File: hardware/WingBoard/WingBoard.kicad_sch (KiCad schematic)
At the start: 12 parts

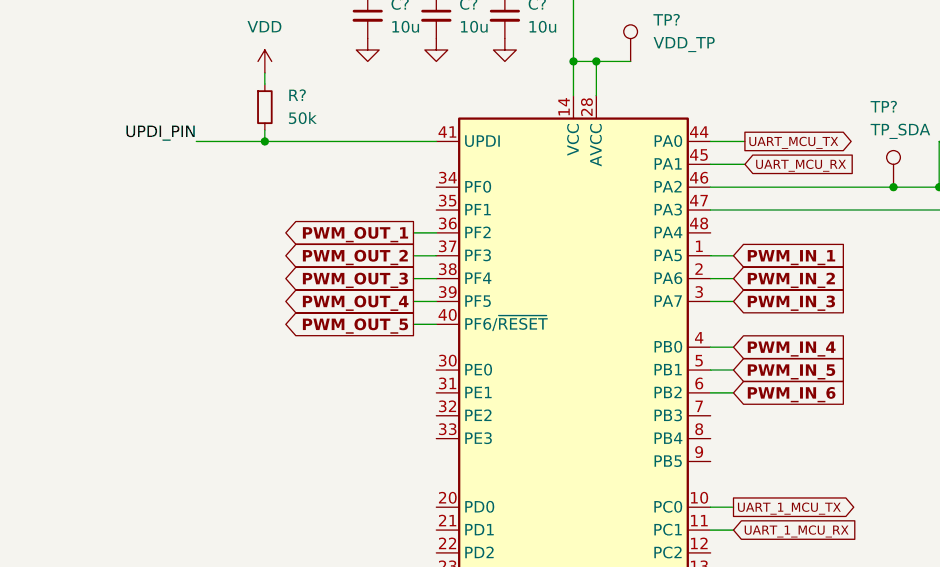
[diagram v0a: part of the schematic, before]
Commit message: Added extra I2C headers to the schematic.
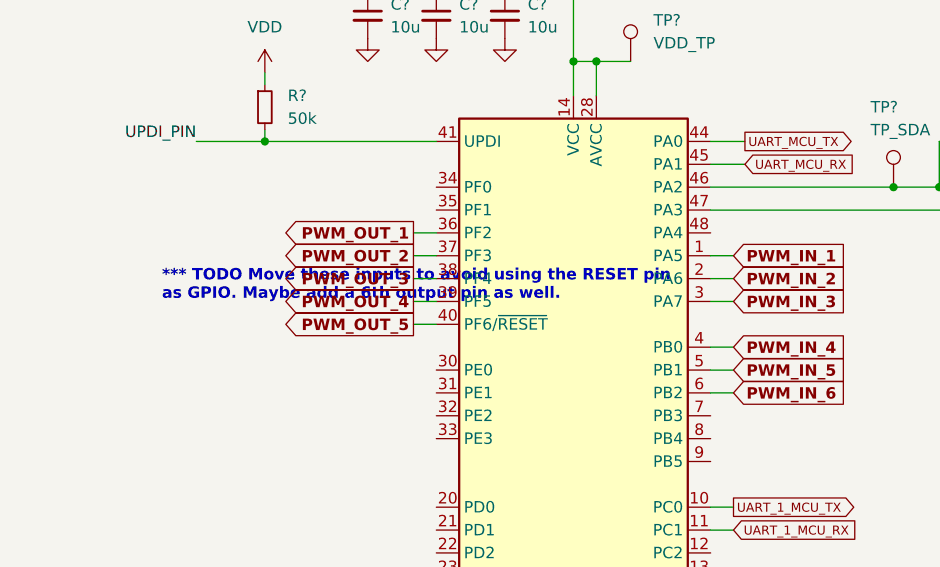
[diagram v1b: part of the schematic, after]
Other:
- note added: "*** TODO Move these inputs to avoid using the RESET pin as GPIO. Maybe add a 6th output pin as well."
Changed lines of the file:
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@@
     (effects (font (size 2 2) bold) (justify left bottom))
+  )
+  (text "*** TODO Move these inputs to avoid using the RESET pin \nas GPIO. Maybe add a 6th output pin as well. "
+    (at 111.76 90.17 0)
+    (effects (font (size 1.27 1.27) bold) (justify left bottom))
   )
   (label "UPDI_PIN" (at 115.57 72.39 180)
@@
       (reference "#PWR?") (unit 1) (value "VDD") (footprint "")
     )
+    (path "/65d0734d-0a9b-4de3-a1fd-6529edb3e633/6a814641-d20c-418e-bbf6-ee1c84b98cad"
+      (reference "#PWR?") (unit 1) (value "VDD") (footprint "")
+    )
     (path "/7d003a0c-bec3-4bcf-bfcd-49935645a638/6fb03914-ff97-4a61-9273-9addb35c7176"
       (reference "#PWR?") (unit 1) (value "VDD") (footprint "")
@@
       (reference "#PWR?") (unit 1) (value "GND") (footprint "")
     )
+    (path "/65d0734d-0a9b-4de3-a1fd-6529edb3e633/caa19d0f-3ce8-416e-bb63-fc48f119bca8"
+      (reference "#PWR?") (unit 1) (value "GND") (footprint "")
+    )
+    (path "/65d0734d-0a9b-4de3-a1fd-6529edb3e633/ccb53472-8d23-471d-b2ec-caf44c144929"
+      (reference "#PWR?") (unit 1) (value "+3.3V") (footprint "")
+    )
+    (path "/65d0734d-0a9b-4de3-a1fd-6529edb3e633/d00ec237-131f-4e59-a480-f807d62e1309"
+      (reference "#PWR?") (unit 1) (value "GND") (footprint "")
+    )
     (path "/4e596909-8b66-4241-be1c-98ec74d77d36/d23c6e59-cc6d-468e-8847-c3cbf6d7174c"
       (reference "#PWR?") (unit 1) (value "GND") (footprint "")
@@
       (reference "J?") (unit 1) (value "PWM_IN2") (footprint "")
     )
+    (path "/65d0734d-0a9b-4de3-a1fd-6529edb3e633/5cc5677a-8af6-4030-9d19-2ee131f6671a"
+      (reference "J?") (unit 1) (value "I2C_X_5V") (footprint "")
+    )
     (path "/4e596909-8b66-4241-be1c-98ec74d77d36/814f2db9-0947-4f62-a212-136e66c5dfa2"
       (reference "J?") (unit 1) (value "PWM_IN1") (footprint "")
@@
       (reference "J?") (unit 1) (value "PWM_IN3") (footprint "")
     )
+    (path "/65d0734d-0a9b-4de3-a1fd-6529edb3e633/f9357d31-2708-45a1-b765-33a95a94766e"
+      (reference "J?") (unit 1) (value "I2C_X_5V") (footprint "")
+    )
     (path "/fd764008-cb4d-4b17-a97c-334a95d80dd4"

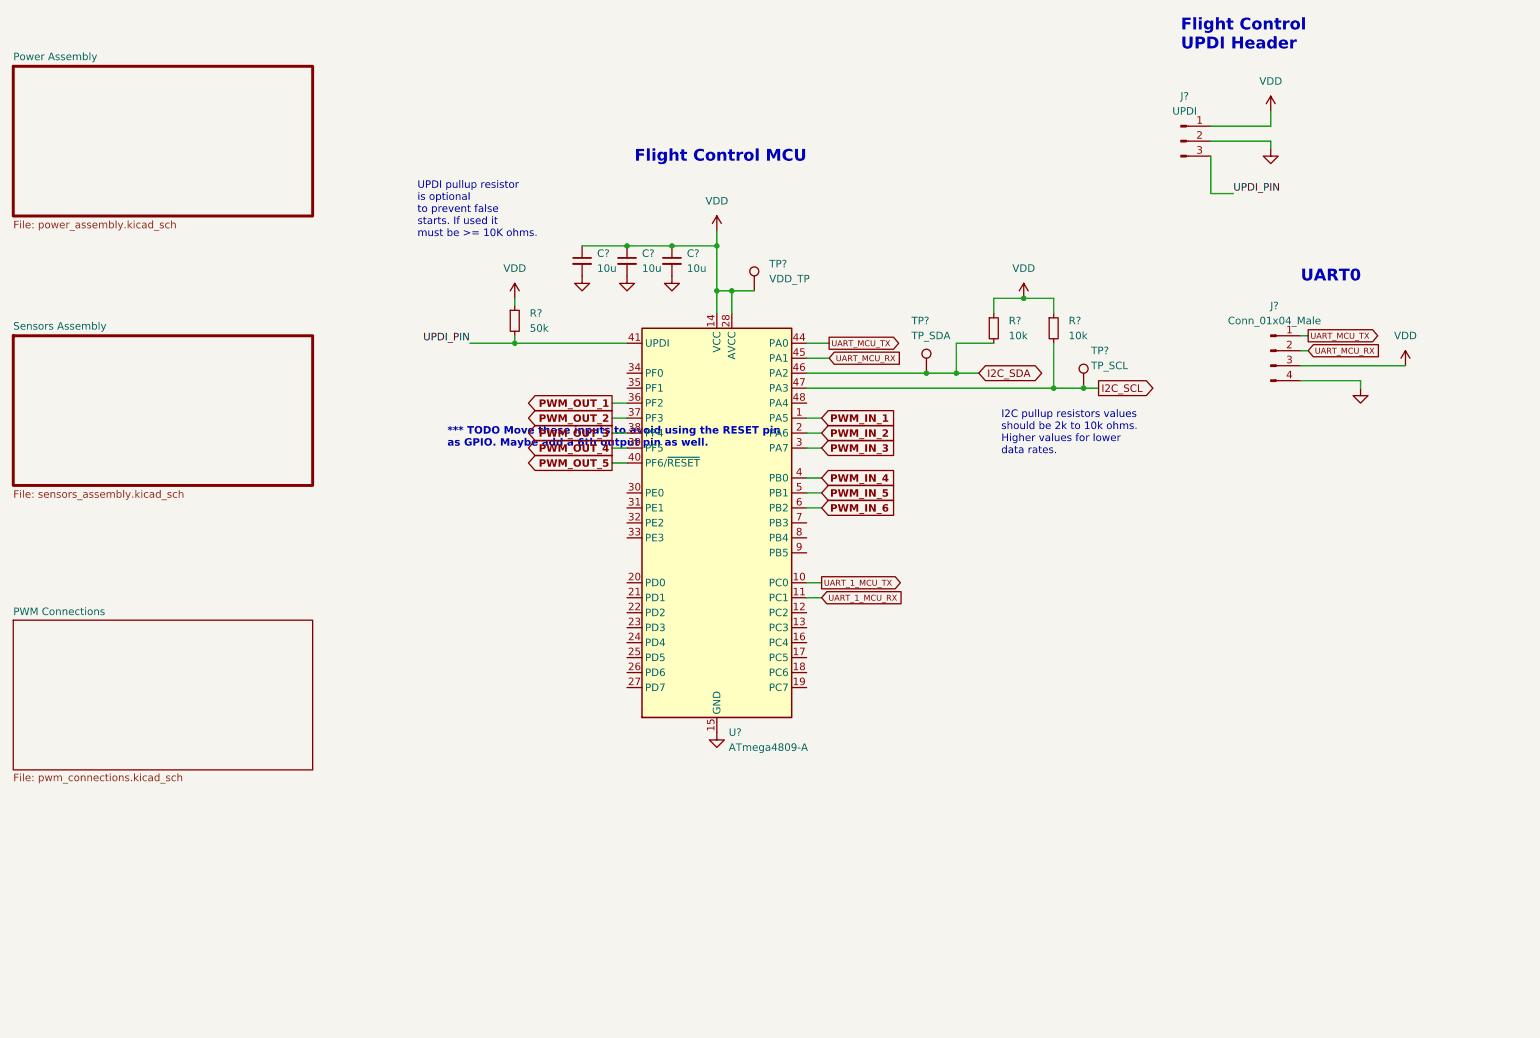
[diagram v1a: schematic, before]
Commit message: Added pwm controller.
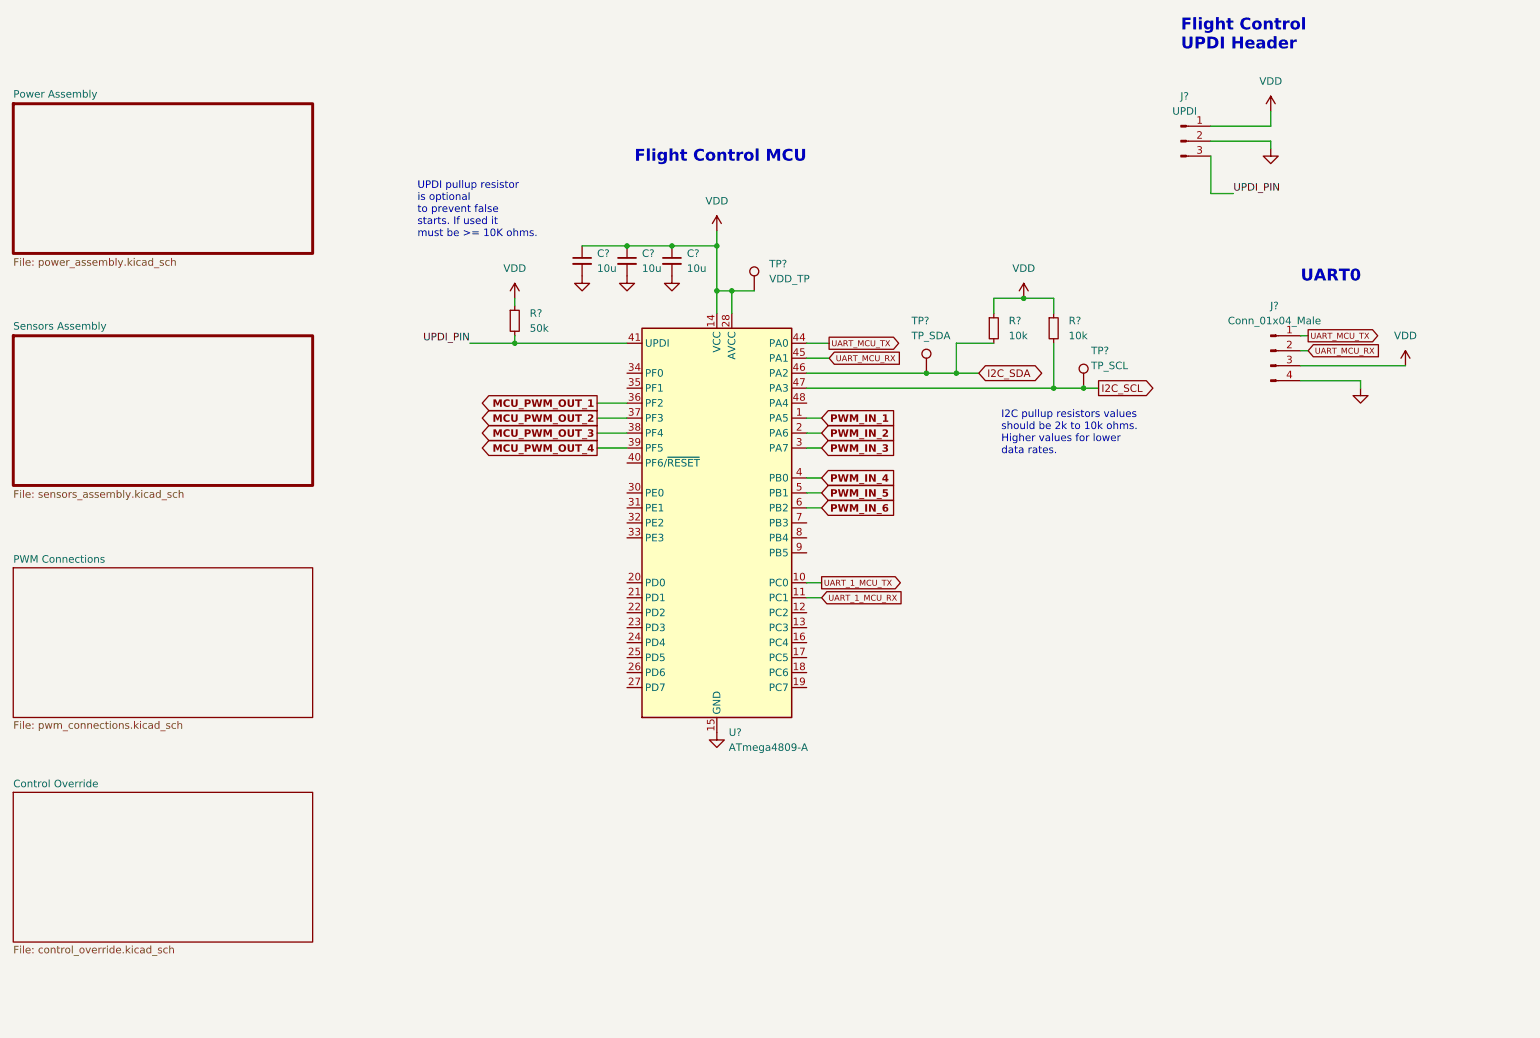
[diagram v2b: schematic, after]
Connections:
- net PWM_OUT_1 renamed MCU_PWM_OUT_1
- net PWM_OUT_2 renamed MCU_PWM_OUT_2
- net PWM_OUT_3 renamed MCU_PWM_OUT_3
- net PWM_OUT_4 renamed MCU_PWM_OUT_4
- net PWM_OUT_5: no longer names the net of U?.40 (PF6/~{RESET})
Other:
- added sheet Control Override (control_override.kicad_sch)
- note removed: "*** TODO Move these inputs to avoid using the RESET pin as GPIO. Maybe add a 6th output pin as well."

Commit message: Hardware update: status LEDs, DIP switches, & test points.
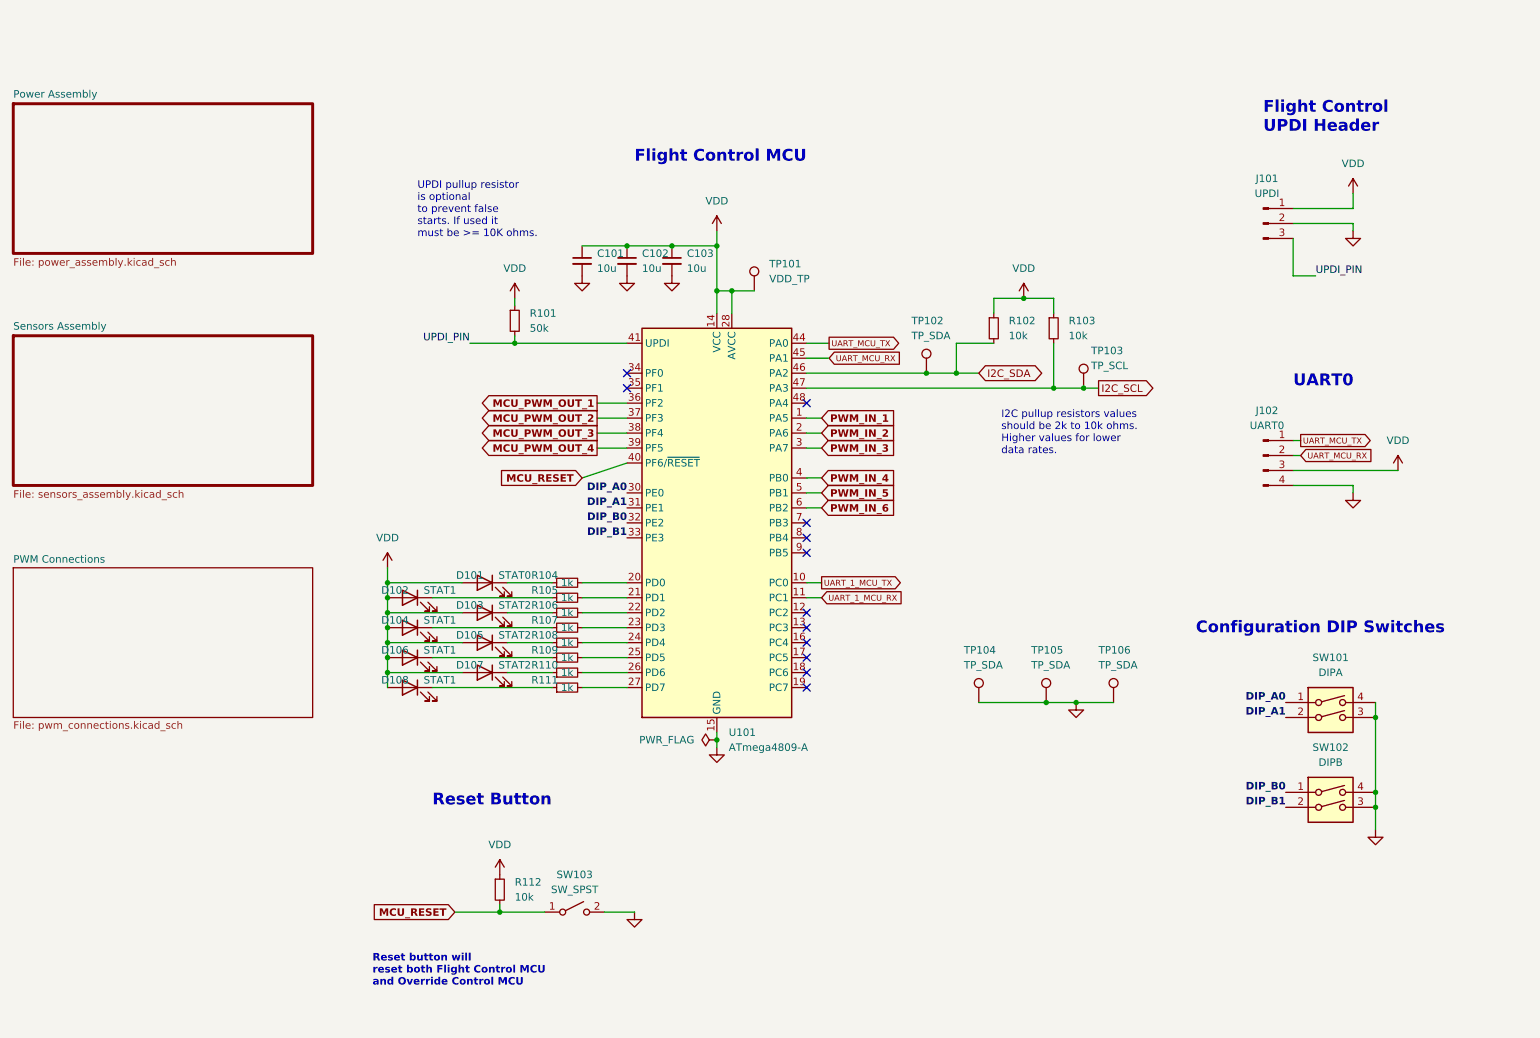
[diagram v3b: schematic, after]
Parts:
- added D101: STAT0, symbol Device:LED
- added D102, D104, D106, D108: STAT1, symbol Device:LED
- added D103, D105, D107: STAT2, symbol Device:LED
- added R104, R105, R106, R107, R108, R109, R110, R111: 1k, symbol Device:R_Small
- added R112: 10k, symbol Device:R_Small
- added SW101: DIPA, symbol Switch:SW_DIP_x02
- added SW102: DIPB, symbol Switch:SW_DIP_x02
- added SW103: SW_SPST, symbol Switch:SW_SPST
- added TP104, TP105, TP106: TP_SDA, symbol Connector:TestPoint
- J102: renamed from J?; value Conn_01x04_Male -> UART0
- gave numbers to parts that had none: 11
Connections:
- net GND: now also SW101.3, SW101.4, SW102.3, SW102.4, SW103.2 (B), TP104.1, TP105.1, TP106.1
- net VDD: now also D101.2 (A), D102.2 (A), D103.2 (A), D104.2 (A), D105.2 (A), D106.2 (A), D107.2 (A), D108.2 (A), R112.1
- net at U101.20 (PD0): now also R104.2
- net at U101.21 (PD1): now also R105.2
- net at U101.22 (PD2): now also R106.2
- net at U101.23 (PD3): now also R107.2
- net at U101.24 (PD4): now also R108.2
- net at U101.25 (PD5): now also R109.2
- net at U101.26 (PD6): now also R110.2
- net at U101.27 (PD7): now also R111.2
- net DIP_A0: now reaches U101.30 (PE0)
- net DIP_A0: now also SW101.1
- net DIP_A1: now reaches U101.31 (PE1)
- net DIP_A1: now also SW101.2
- net DIP_B0: now reaches U101.32 (PE2)
- net DIP_B0: now also SW102.1
- net DIP_B1: now reaches U101.33 (PE3)
- net DIP_B1: now also SW102.2
- net MCU_RESET: now reaches U101.40 (PF6/~{RESET})
- net MCU_RESET: now also R112.2, SW103.1 (A)
- new net: D102.1 (K), R105.1
- new net: D107.1 (K), R110.1
- new net: D104.1 (K), R107.1
- new net: D108.1 (K), R111.1
- new net: D106.1 (K), R109.1
- new net: D101.1 (K), R104.1
- new net: D103.1 (K), R106.1
- new net: D105.1 (K), R108.1
- no-connect marks 0 -> 12
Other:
- removed sheet Control Override
- note added: "Configuration DIP Switches"
- note added: "Reset Button"
- note added: "Reset button will reset both Flight Control MCU and Override Control MCU"
- moved on the sheet: J101, J102

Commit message: Minor hardware design updates and assigned PCB footprints
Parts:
- C101, C102, C103: value 10u -> 100n; footprint (none) -> Capacitor_SMD:C_0805_2012Metric_Pad1.18x1.45mm_HandSolder
- D101, D102, D103, D104, D105, D106, D107, D108: footprint (none) -> LED_SMD:LED_0805_2012Metric_Pad1.15x1.40mm_HandSolder
- J101: footprint (none) -> Connector_PinHeader_2.54mm:PinHeader_1x03_P2.54mm_Vertical
- J102: footprint (none) -> Connector_JST:JST_SH_BM04B-SRSS-TB_1x04-1MP_P1.00mm_Vertical
- R101, R102, R103, R104, R105, R106, R107, R108, R109, R110, R111, R112: footprint (none) -> Resistor_SMD:R_0805_2012Metric_Pad1.20x1.40mm_HandSolder
- SW101, SW102: footprint (none) -> Button_Switch_SMD:SW_DIP_SPSTx02_Slide_Copal_CHS-02B_W7.62mm_P1.27mm
- SW103: footprint (none) -> Switch:R-668127
- TP101, TP102, TP103, TP104, TP105, TP106: footprint (none) -> TestPoint:TestPoint_Pad_D1.5mm

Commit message: PCB rough layout done.
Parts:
- added H101, H102, H103, H104: MountingHole, MountingHole:MountingHole_3mm_Pad_Via, symbol Mechanical:MountingHole
- D104: value STAT1 -> STAT3
- D105: value STAT2 -> STAT4
- D106: value STAT1 -> STAT5
- D107: value STAT2 -> STAT6
- D108: value STAT1 -> STAT7
- J102: footprint Connector_JST:JST_SH_BM04B-SRSS-TB_1x04-1MP_P1.00mm_Vertical -> Connector_PinHeader_2.54mm:PinHeader_1x04_P2.54mm_Vertical
- TP104, TP105, TP106: value TP_SDA -> TP_GND
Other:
- note added: "The DIP switches have no specific purpose at this time but could be handy for making configuration changes on the fly."
- note added: "UART0 is intended for diagnostic and debug print statments."
- moved on the sheet: SW101, SW102, TP104, TP105, TP106

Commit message: Hardware layout v0.1 complete.
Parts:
- removed D101: STAT0, LED_SMD:LED_0805_2012Metric_Pad1.15x1.40mm_HandSolder, symbol Device:LED
- removed D102: STAT1, LED_SMD:LED_0805_2012Metric_Pad1.15x1.40mm_HandSolder, symbol Device:LED
- removed D103: STAT2, LED_SMD:LED_0805_2012Metric_Pad1.15x1.40mm_HandSolder, symbol Device:LED
- removed D104: STAT3, LED_SMD:LED_0805_2012Metric_Pad1.15x1.40mm_HandSolder, symbol Device:LED
- removed R104, R105, R106, R107: 1k, Resistor_SMD:R_0805_2012Metric_Pad1.20x1.40mm_HandSolder, symbol Device:R_Small
- removed SW102: DIPB, Button_Switch_SMD:SW_DIP_SPSTx02_Slide_Copal_CHS-02B_W7.62mm_P1.27mm, symbol Switch:SW_DIP_x02
- removed TP101: VDD_TP, TestPoint:TestPoint_Pad_D1.5mm, symbol Connector:TestPoint
- removed TP105, TP106: TP_GND, TestPoint:TestPoint_Pad_D1.5mm, symbol Connector:TestPoint
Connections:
- net DIP_A0: now also U101.36 (PF2); no longer U101.30 (PE0)
- net DIP_A1: now also U101.35 (PF1); no longer U101.31 (PE1)
- net MCU_PWM_OUT_1: now also U101.19 (PC7); no longer U101.36 (PF2)
- net MCU_PWM_OUT_2: now also U101.18 (PC6); no longer U101.37 (PF3)
- net MCU_PWM_OUT_3: now also U101.17 (PC5); no longer U101.38 (PF4)
- net MCU_PWM_OUT_4: now also U101.16 (PC4); no longer U101.39 (PF5)
- net VDD: now also R108.1, R109.1, R110.1, R111.1; no longer D105.2 (A), D106.2 (A), D107.2 (A), D108.2 (A)
- net STAT_2: now reaches U101.21 (PD1)
- net STAT_2: now also D107.1 (K)
- net at R110.2: now also D107.2 (A); no longer U101.26 (PD6)
- net STAT_1: now reaches D108.1 (K)
- net STAT_1: now also U101.20 (PD0); no longer R111.1
- net at R111.2: now also D108.2 (A); no longer U101.27 (PD7)
- net STAT_3: now reaches D106.1 (K)
- net STAT_3: now also U101.22 (PD2); no longer R109.1
- net STAT_4: now reaches U101.23 (PD3)
- net STAT_4: now also D105.1 (K)
- net at R109.2: now also D106.2 (A); no longer U101.25 (PD5)
- net at R108.2: now also D105.2 (A); no longer U101.24 (PD4)
- net DIP_B0: no longer names the net of U101.32 (PE2)
- net DIP_B1: no longer names the net of U101.33 (PE3)
- no-connect marks 12 -> 14
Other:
- note added: "Status LEDs"
- note added: "The DIP switches and status lights have no specific purpose at this time but could be handy for making configuration changes on the fly."
- note removed: "The DIP switches have no specific purpose at this time but could be handy for making configuration changes on the fly."
- moved on the sheet: D105, D106, D107, D108, J101, J102, R108, R109, R110, R111, R112, SW101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
